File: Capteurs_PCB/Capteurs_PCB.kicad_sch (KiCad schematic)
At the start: 17 parts, among them J1 Conn_01x04, J101 Conn_01x03, J103 Conn_02x20_Odd_Even, J104 Conn_ST_STDC14, J2 Conn_01x03, J3 Alim_Prop1, J5 Alim_Prop1, SW101 SW_DPDT_x2, U1 STM32L412KBTx

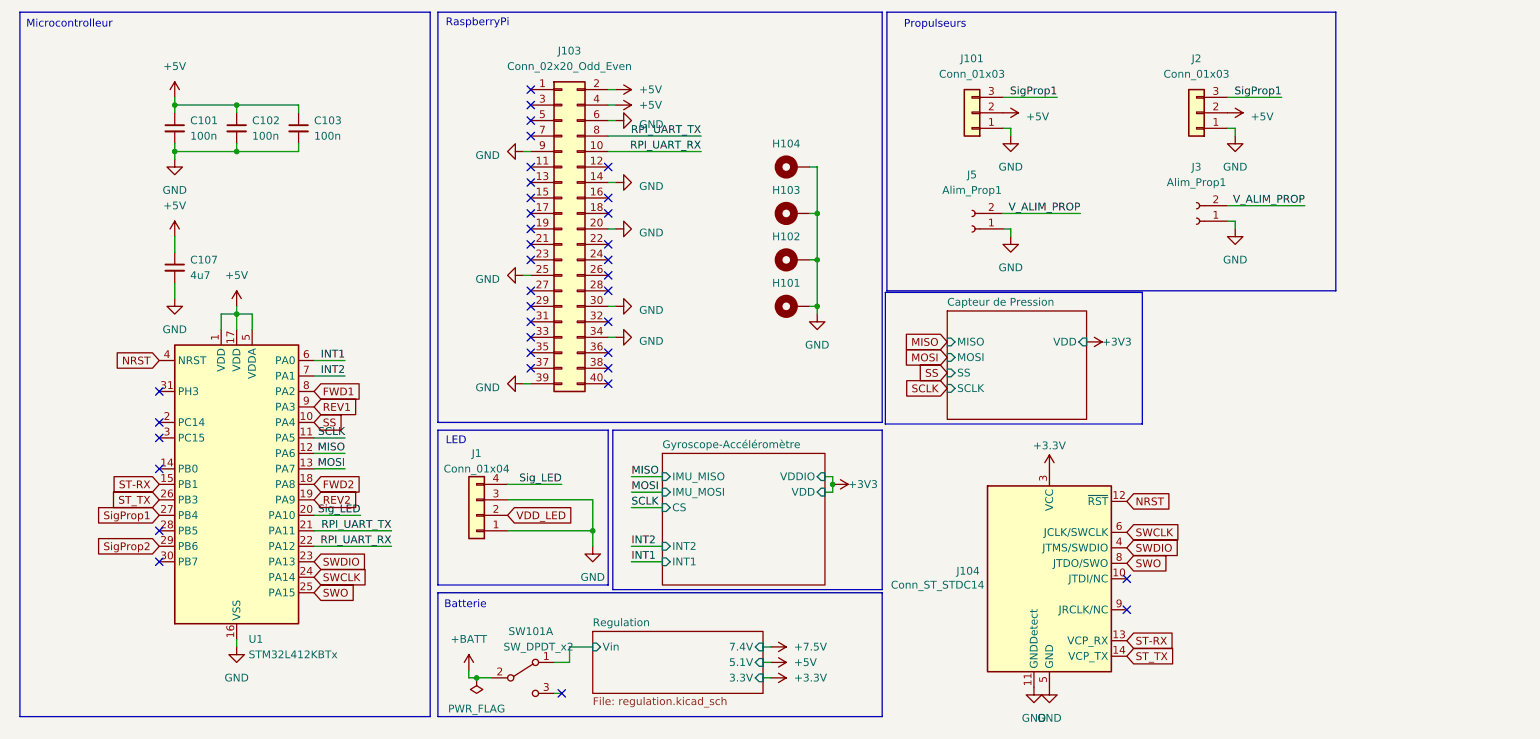
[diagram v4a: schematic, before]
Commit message: Enlever les erreurs Kicad+Mettre connecteur batterie
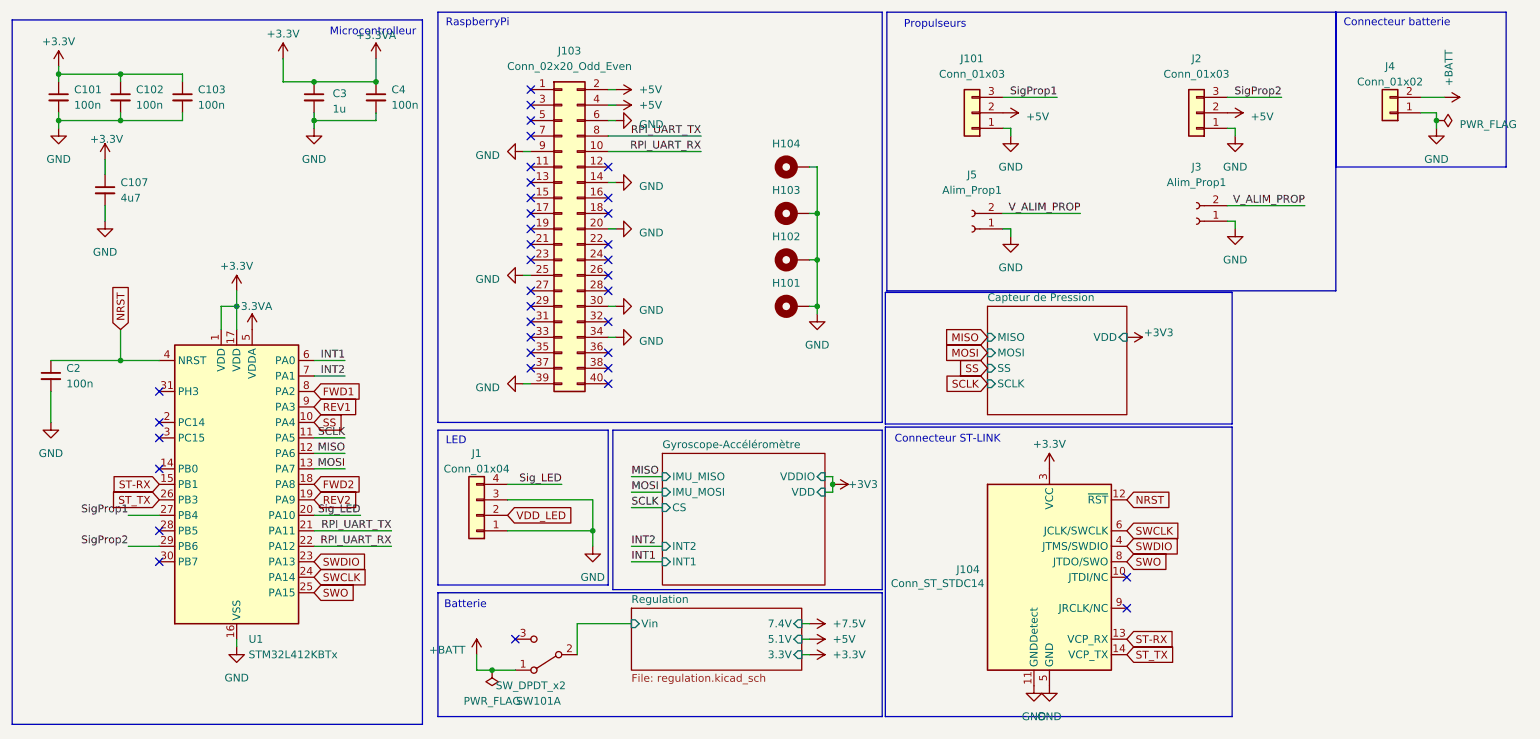
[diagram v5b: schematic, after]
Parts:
- added C2, C4: 100n, Capacitor_SMD:C_1206_3216Metric, symbol Device:C_Small
- added C3: 1u, Capacitor_SMD:C_1206_3216Metric, symbol Device:C_Small
- added J4: Conn_01x02, symbol Connector_Generic:Conn_01x02
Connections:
- net +3.3V: now also C101.1, C102.1, C103.1, C107.1, U1.1 (VDD), U1.17 (VDD), U1.5 (VDDA), C3.1, C4.1
- net +5V: no longer C101.1, C102.1, C103.1, C107.1, U1.1 (VDD), U1.17 (VDD), U1.5 (VDDA)
- net +BATT: now also SW101.1 (A), J4.2 (Pin_2); no longer SW101.2 (B)
- net GND: now also C2.2, C3.2, C4.2, J4.1 (Pin_1)
- net NRST: now also C2.1
- net Regulation/Vin: now also SW101.2 (B); no longer SW101.1 (A)
- net SigProp1: no longer J2.3 (Pin_3)
- net SigProp2: now also J2.3 (Pin_3)
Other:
- note added: "Connecteur ST-LINK"
- note added: "Connecteur batterie"
- moved on the sheet: C101, C102, C103, C107, SW101A

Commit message: Kicad
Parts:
- added J6, J7: Conn_01x02, symbol Connector_Generic:Conn_01x02
- added L1: 39n, symbol Device:L
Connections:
- net +3.3V: now also L1.1; no longer C3.1, C4.1, U1.5 (VDDA)
- net +BATT: now also SW101.3 (C); no longer SW101.1 (A)
- net FWD1: now also J6.2 (Pin_2)
- net FWD2: now also J7.2 (Pin_2)
- net REV1: now also J6.1 (Pin_1)
- net REV2: now also J7.1 (Pin_1)
- new net +3.3VA: C3.1, C4.1, L1.2, U1.5 (VDDA)
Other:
- note added: "Moteur"

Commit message: Empreintes
A revoir car pas sur pour certaines + faire celles des composants modifiés
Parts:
- J1: footprint (none) -> Connector_PinSocket_2.54mm:PinSocket_1x04_P2.54mm_Vertical
- J101: footprint (none) -> Connector_PinHeader_2.54mm:PinHeader_1x03_P2.54mm_Vertical
- J103: footprint (none) -> Connector_PinSocket_2.54mm:PinSocket_2x20_P2.54mm_Vertical
- J104: footprint (none) -> Connector_PinHeader_1.27mm:PinHeader_2x07_P1.27mm_Vertical
- J2: footprint (none) -> Connector_PinSocket_2.54mm:PinSocket_1x03_P2.54mm_Vertical
- J4, J6, J7: footprint (none) -> Connector_PinHeader_2.54mm:PinHeader_1x02_P2.54mm_Vertical
- L1: footprint (none) -> Inductor_SMD:L_0805_2012Metric
- SW101: footprint (none) -> Button_Switch_SMD:SW_DPDT_CK_JS202011JCQN
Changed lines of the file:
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@@
       (effects (font (size 1.27 1.27)) (justify right))
     )
-    (property "Footprint" "" (at 182.88 106.68 0)
+    (property "Footprint" "Connector_PinHeader_1.27mm:PinHeader_2x07_P1.27mm_Vertical" (at 182.88 106.68 0)
       (effects (font (size 1.27 1.27)) hide)
     )
@@
       (effects (font (size 1.27 1.27)))
     )
-    (property "Footprint" "" (at 219.71 74.93 0)
+    (property "Footprint" "Connector_PinHeader_2.54mm:PinHeader_1x02_P2.54mm_Vertical" (at 219.71 74.93 0)
       (effects (font (size 1.27 1.27)) hide)
     )
@@
       (effects (font (size 1.27 1.27)))
     )
-    (property "Footprint" "" (at 102.87 49.53 0)
+    (property "Footprint" "Connector_PinSocket_2.54mm:PinSocket_2x20_P2.54mm_Vertical" (at 102.87 49.53 0)
       (effects (font (size 1.27 1.27)) hide)
     )
@@
       (effects (font (size 1.27 1.27)))
     )
-    (property "Footprint" "" (at 207.01 30.48 0)
+    (property "Footprint" "Connector_PinSocket_2.54mm:PinSocket_1x03_P2.54mm_Vertical" (at 207.01 30.48 0)
       (effects (font (size 1.27 1.27)) hide)
     )
@@
       (effects (font (size 1.27 1.27)))
     )
-    (property "Footprint" "" (at 238.76 30.48 0)
+    (property "Footprint" "Connector_PinHeader_2.54mm:PinHeader_1x02_P2.54mm_Vertical" (at 238.76 30.48 0)
       (effects (font (size 1.27 1.27)) hide)
     )
@@
       (effects (font (size 1.27 1.27)))
     )
-    (property "Footprint" "" (at 241.3 74.93 0)
+    (property "Footprint" "Connector_PinHeader_2.54mm:PinHeader_1x02_P2.54mm_Vertical" (at 241.3 74.93 0)
       (effects (font (size 1.27 1.27)) hide)
     )
@@
       (effects (font (size 1.27 1.27)))
     )
-    (property "Footprint" "" (at 100.33 119.38 0)
+    (property "Footprint" "Button_Switch_SMD:SW_DPDT_CK_JS202011JCQN" (at 100.33 119.38 0)
       (effects (font (size 1.27 1.27)) hide)
     )
@@
       (effects (font (size 1.27 1.27)))
     )
-    (property "Footprint" "" (at 55.88 25.4 0)
+    (property "Footprint" "Inductor_SMD:L_0805_2012Metric" (at 55.88 25.4 0)
       (effects (font (size 1.27 1.27)) hide)
     )
@@
       (effects (font (size 1.27 1.27)))
     )
-    (property "Footprint" "" (at 170.18 30.48 0)
+    (property "Footprint" "Connector_PinHeader_2.54mm:PinHeader_1x03_P2.54mm_Vertical" (at 170.18 30.48 0)
       (effects (font (size 1.27 1.27)) hide)
     )
@@
       (effects (font (size 1.27 1.27)))
     )
-    (property "Footprint" "" (at 88.9 96.52 0)
-      (effects (font (size 1.27 1.27)) hide)
-    )
+    (property "Footprint" "Connector_PinSocket_2.54mm:PinSocket_1x04_P2.54mm_Vertical" (at 88.9 96.52 0)
+      (effects (font (size 1.27 1.27)) hide)
+    )

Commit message: Empreintes modifiées
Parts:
- C101, C102, C103, C107, C2, C3, C4: footprint Capacitor_SMD:C_1206_3216Metric -> Capacitor_SMD:C_1206_3216Metric_Pad1.33x1.80mm_HandSolder
- H101, H102, H103, H104: footprint (none) -> MountingHole:MountingHole_3.2mm_M3_DIN965_Pad
- L1: footprint Inductor_SMD:L_0805_2012Metric -> Inductor_SMD:L_0805_2012Metric_Pad1.05x1.20mm_HandSolder
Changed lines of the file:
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@@
       (effects (font (size 1.27 1.27)) (justify left))
     )
-    (property "Footprint" "Capacitor_SMD:C_1206_3216Metric" (at 27.94 43.18 0)
+    (property "Footprint" "Capacitor_SMD:C_1206_3216Metric_Pad1.33x1.80mm_HandSolder" (at 27.94 43.18 0)
       (effects (font (size 1.27 1.27)) hide)
     )
@@
       (effects (font (size 1.27 1.27)) hide)
     )
-    (property "Footprint" "" (at 140.97 54.61 0)
+    (property "Footprint" "MountingHole:MountingHole_3.2mm_M3_DIN965_Pad" (at 140.97 54.61 0)
       (effects (font (size 1.27 1.27)) hide)
     )
@@
       (effects (font (size 1.27 1.27)) (justify left))
     )
-    (property "Footprint" "Capacitor_SMD:C_1206_3216Metric" (at 20.32 27.94 0)
+    (property "Footprint" "Capacitor_SMD:C_1206_3216Metric_Pad1.33x1.80mm_HandSolder" (at 20.32 27.94 0)
       (effects (font (size 1.27 1.27)) hide)
     )
@@
       (effects (font (size 1.27 1.27)) hide)
     )
-    (property "Footprint" "" (at 140.97 46.99 0)
+    (property "Footprint" "MountingHole:MountingHole_3.2mm_M3_DIN965_Pad" (at 140.97 46.99 0)
       (effects (font (size 1.27 1.27)) hide)
     )
@@
       (effects (font (size 1.27 1.27)) hide)
     )
-    (property "Footprint" "" (at 140.97 62.23 0)
+    (property "Footprint" "MountingHole:MountingHole_3.2mm_M3_DIN965_Pad" (at 140.97 62.23 0)
       (effects (font (size 1.27 1.27)) hide)
     )
@@
       (effects (font (size 1.27 1.27)) (justify left))
     )
-    (property "Footprint" "Capacitor_SMD:C_1206_3216Metric" (at 72.39 27.94 0)
+    (property "Footprint" "Capacitor_SMD:C_1206_3216Metric_Pad1.33x1.80mm_HandSolder" (at 72.39 27.94 0)
       (effects (font (size 1.27 1.27)) hide)
     )
@@
       (effects (font (size 1.27 1.27)) (justify left))
     )
-    (property "Footprint" "Capacitor_SMD:C_1206_3216Metric" (at 40.64 27.94 0)
+    (property "Footprint" "Capacitor_SMD:C_1206_3216Metric_Pad1.33x1.80mm_HandSolder" (at 40.64 27.94 0)
       (effects (font (size 1.27 1.27)) hide)
     )
@@
       (effects (font (size 1.27 1.27)))
     )
-    (property "Footprint" "Inductor_SMD:L_0805_2012Metric" (at 55.88 25.4 0)
+    (property "Footprint" "Inductor_SMD:L_0805_2012Metric_Pad1.05x1.20mm_HandSolder" (at 55.88 25.4 0)
       (effects (font (size 1.27 1.27)) hide)
     )
@@
       (effects (font (size 1.27 1.27)) (justify left))
     )
-    (property "Footprint" "Capacitor_SMD:C_1206_3216Metric" (at 62.23 27.94 0)
+    (property "Footprint" "Capacitor_SMD:C_1206_3216Metric_Pad1.33x1.80mm_HandSolder" (at 62.23 27.94 0)
       (effects (font (size 1.27 1.27)) hide)
     )
@@
       (effects (font (size 1.27 1.27)) (justify left))
     )
-    (property "Footprint" "Capacitor_SMD:C_1206_3216Metric" (at 19.05 73.66 0)
+    (property "Footprint" "Capacitor_SMD:C_1206_3216Metric_Pad1.33x1.80mm_HandSolder" (at 19.05 73.66 0)
       (effects (font (size 1.27 1.27)) hide)
     )
@@
       (effects (font (size 1.27 1.27)) (justify left))
     )
-    (property "Footprint" "Capacitor_SMD:C_1206_3216Metric" (at 30.48 27.94 0)
+    (property "Footprint" "Capacitor_SMD:C_1206_3216Metric_Pad1.33x1.80mm_HandSolder" (at 30.48 27.94 0)
       (effects (font (size 1.27 1.27)) hide)
     )
@@
       (effects (font (size 1.27 1.27)) hide)
     )
-    (property "Footprint" "" (at 140.97 39.37 0)
-      (effects (font (size 1.27 1.27)) hide)
-    )
+    (property "Footprint" "MountingHole:MountingHole_3.2mm_M3_DIN965_Pad" (at 140.97 39.37 0)
+      (effects (font (size 1.27 1.27)) hide)
+    )
